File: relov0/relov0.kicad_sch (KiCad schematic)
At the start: 0 parts

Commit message: agregar archivos de kicad a gitignore
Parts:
- added C1, C6: 47u, symbol Device:C_Polarized
- added C2: 100u, symbol Device:C_Polarized
- added C3: 100n, Capacitor_THT:C_Disc_D5.0mm_W2.5mm_P2.50mm, symbol Device:C
- added C4: 10u, symbol Device:C_Polarized
- added C5: 100n, symbol Device:C
- added D1: 1N4007, Diode_THT:D_DO-41_SOD81_P10.16mm_Horizontal, symbol Diode:1N4007
- added D2, D3: LED, symbol Device:LED
- added J1, J2: Barrel_Jack_Switch, symbol Connector:Barrel_Jack_Switch
- added J3: salida, symbol Connector_Audio:AudioJack2_SwitchT
- added R1, R2, R3: 1k, symbol Device:R
- added RV1: 100k, symbol Device:R_Potentiometer
- added SW1: SW_SPDT, symbol Switch:SW_SPDT
- added U1: NE555P, Package_DIP:DIP-8_W7.62mm, symbol Timer:NE555P
- added U2: L7805, symbol Regulator_Linear:L7805
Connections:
- new net: D3.1 (K), R3.1
- new net: C6.1, R2.1, U1.3 (OUT)
- new net: D2.2 (A), R2.2
- new net: D1.2 (A), SW1.2 (B)
- new net: C1.1, RV1.3, U1.2 (TRIG), U1.6 (THRES)
- new net: C3.2, U1.5 (CONT)
- new net: R1.1, RV1.2, U1.7 (DISCH)
- new net: J1.1, J2.1, SW1.1 (A)
- new net +12V: C2.1, D1.1 (K), U2.1 (IN)
- new net +5V: C4.1, C5.1, D3.2 (A), R1.2, U1.4 (~{RST}), U1.8 (VCC), U2.3 (OUT)
- new net GND: C1.2, C2.2, C3.1, C4.2, C5.2, D2.1 (K), J1.2, J2.2, R3.2, U1.1 (GND), U2.2 (GND)
- no-connect marks 0 -> 3
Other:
- note added: "chip 555 1 - conectada a tierra 2 - conectada a 6 3 - conectada a tierra a través de un LED protegido por un resistor, y a salida a través de un capacitor 4 - conectada a vcc 5 - conectada a tierra a través de un capacitor 6 - conectada a 2 7 - conectada a vcc a través de un resistor, y a 2 a través de un resistor 8 - conectada a vcc"
- company: (none) -> piruetas SpA
- title: (none) -> relo

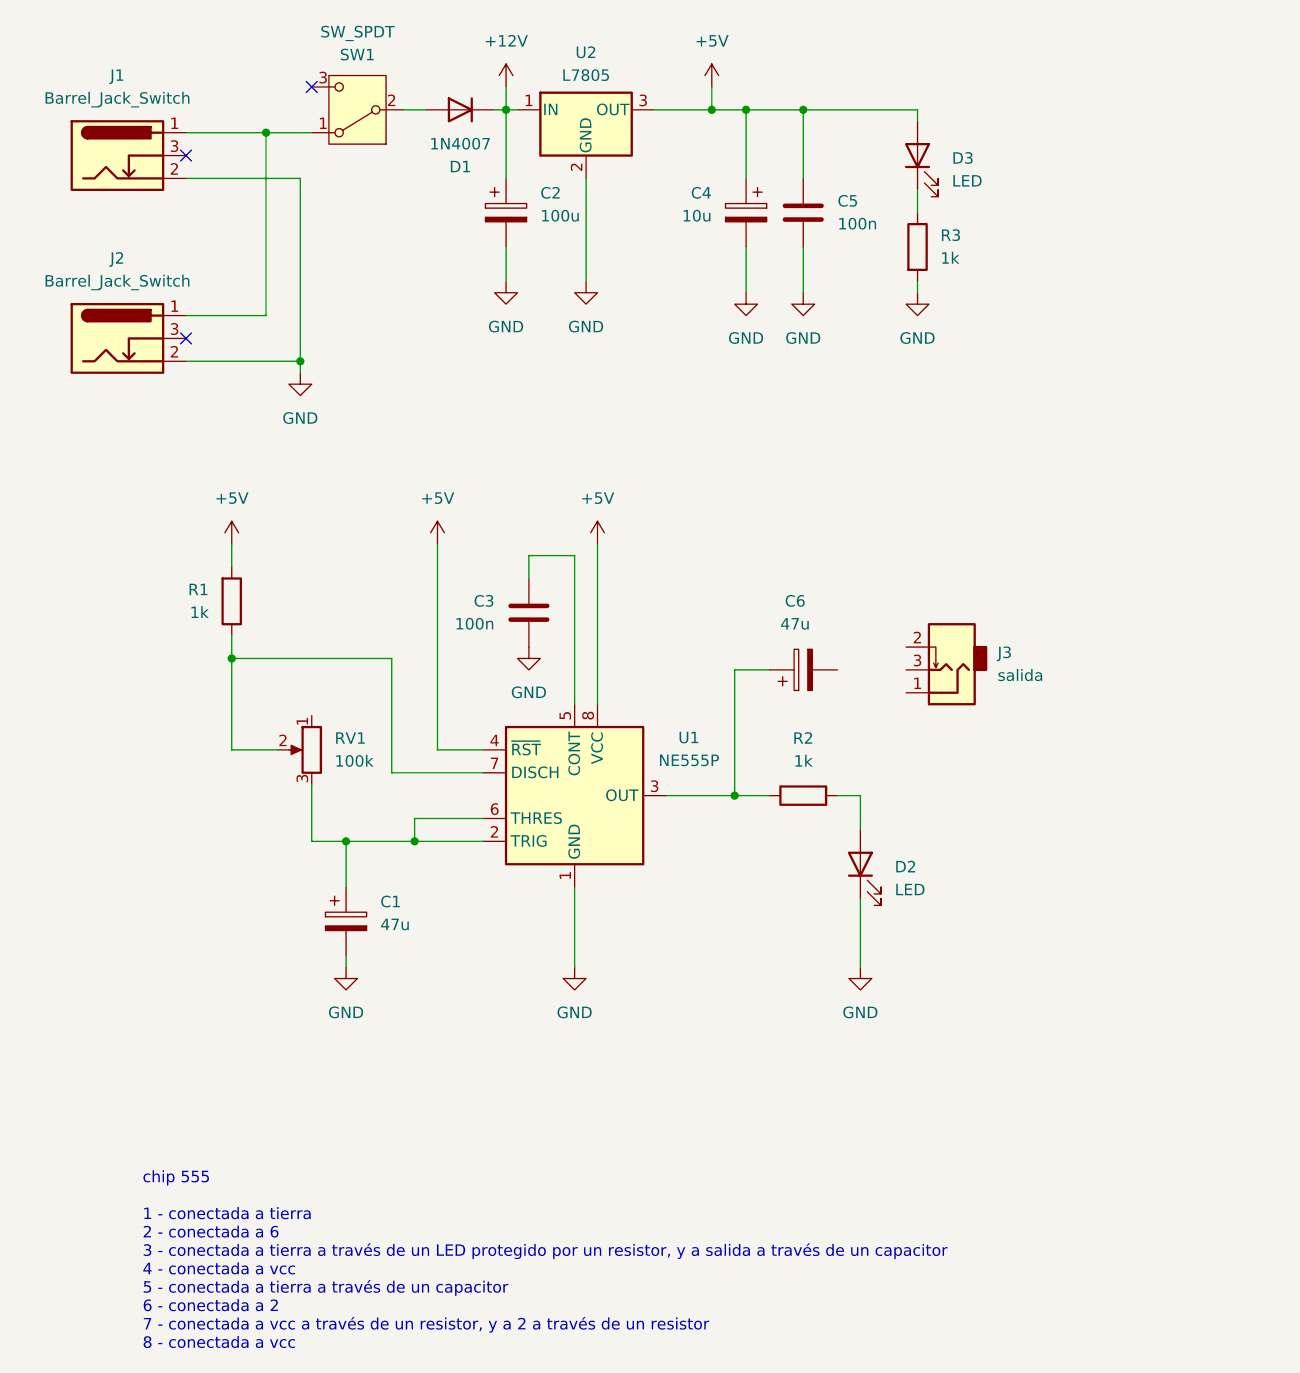
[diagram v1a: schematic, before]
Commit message: agregar biblioteca relo y actualizar footprints
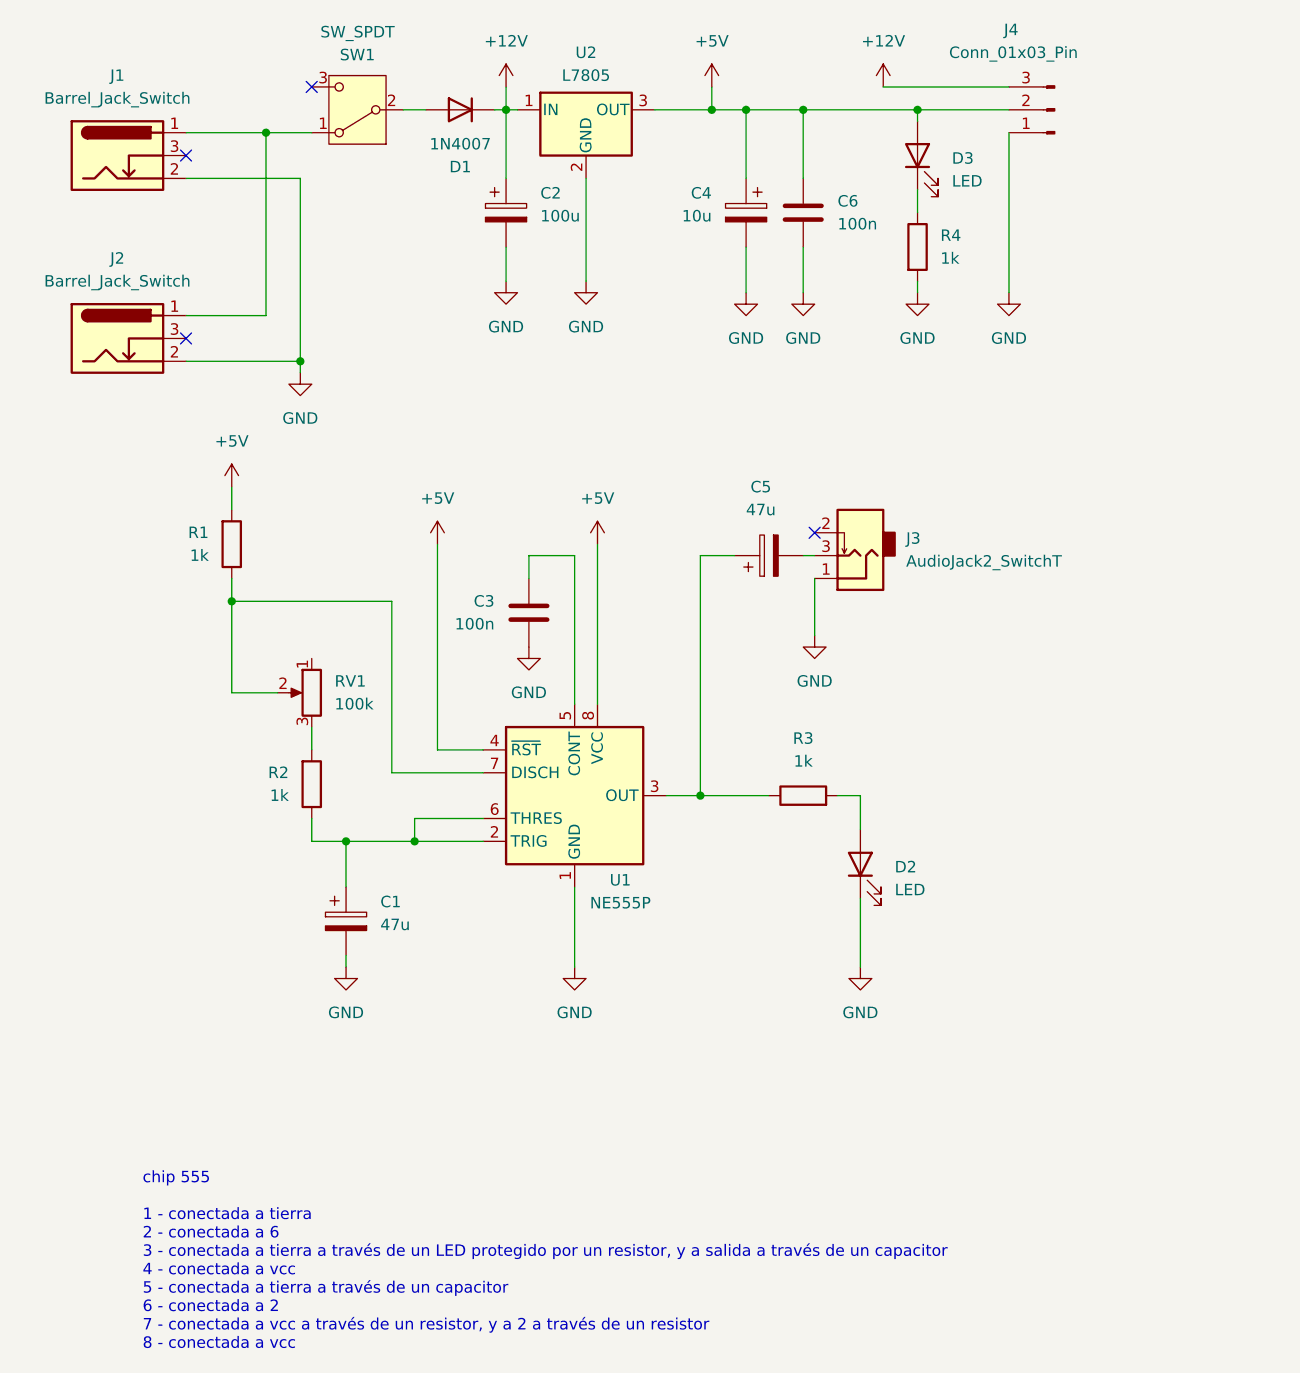
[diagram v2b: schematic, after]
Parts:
- added J4: Conn_01x03_Pin, Connector_PinSocket_2.54mm:PinSocket_1x03_P2.54mm_Vertical, symbol Connector:Conn_01x03_Pin
- added R2: 1k, Resistor_THT:R_Axial_DIN0207_L6.3mm_D2.5mm_P10.16mm_Horizontal, symbol Device:R
- C1: footprint (none) -> Capacitor_THT:CP_Radial_D5.0mm_P2.00mm
- C2: footprint (none) -> Capacitor_THT:CP_Radial_D8.0mm_P3.80mm
- C4: footprint (none) -> Capacitor_THT:CP_Radial_D4.0mm_P2.00mm
- C5: renamed from C6; footprint (none) -> Capacitor_THT:CP_Radial_D5.0mm_P2.00mm
- C6: renamed from C5; footprint (none) -> Capacitor_THT:C_Disc_D5.0mm_W2.5mm_P2.50mm
- D2, D3: footprint (none) -> LED_THT:LED_D5.0mm
- J1, J2: footprint (none) -> Connector_BarrelJack:BarrelJack_Horizontal
- J3: value salida -> AudioJack2_SwitchT; footprint (none) -> relo:PJ301M-12
- R1: footprint (none) -> Resistor_THT:R_Axial_DIN0207_L6.3mm_D2.5mm_P10.16mm_Horizontal
- R3: renamed from R2; footprint (none) -> Resistor_THT:R_Axial_DIN0207_L6.3mm_D2.5mm_P10.16mm_Horizontal
- R4: renamed from R3; footprint (none) -> Resistor_THT:R_Axial_DIN0207_L6.3mm_D2.5mm_P10.16mm_Horizontal
- RV1: footprint (none) -> Potentiometer_THT:Potentiometer_Alps_RK163_Single_Horizontal
- SW1: footprint (none) -> Button_Switch_THT:SW_Slide_SPDT_Straight_CK_OS102011MS2Q
- U1: footprint Package_DIP:DIP-8_W7.62mm -> Package_DIP:DIP-8_W7.62mm_Socket_LongPads
- U2: footprint (none) -> Package_TO_SOT_THT:TO-220-3_Horizontal_TabDown
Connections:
- net +12V: now also J4.3 (Pin_3)
- net +5V: now also J4.2 (Pin_2)
- net GND: now also J3.1, J4.1 (Pin_1)
- net at C1.1, U1.2 (TRIG), U1.6 (THRES): now also R2.1; no longer RV1.3
- net at C5.2: now also J3.3
- new net: R2.2, RV1.3
- no-connect marks 3 -> 4
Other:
- moved on the sheet: C5, J3, R1, RV1

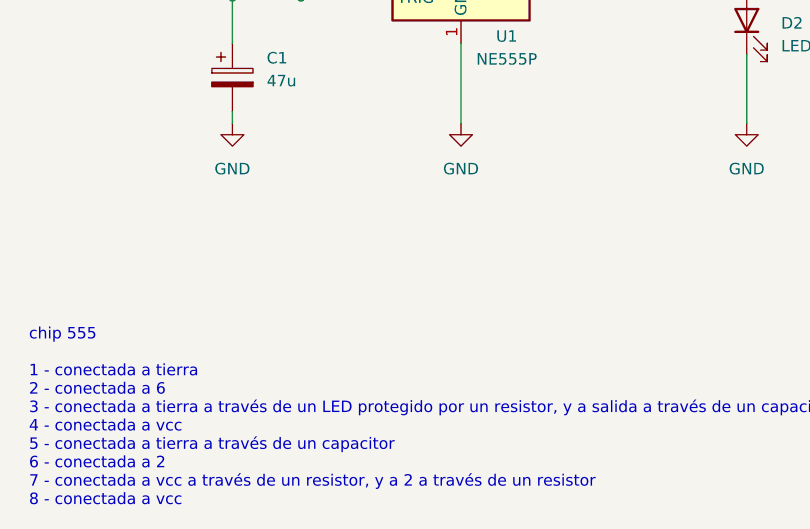
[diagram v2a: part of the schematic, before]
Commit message: agregar nuevas mods
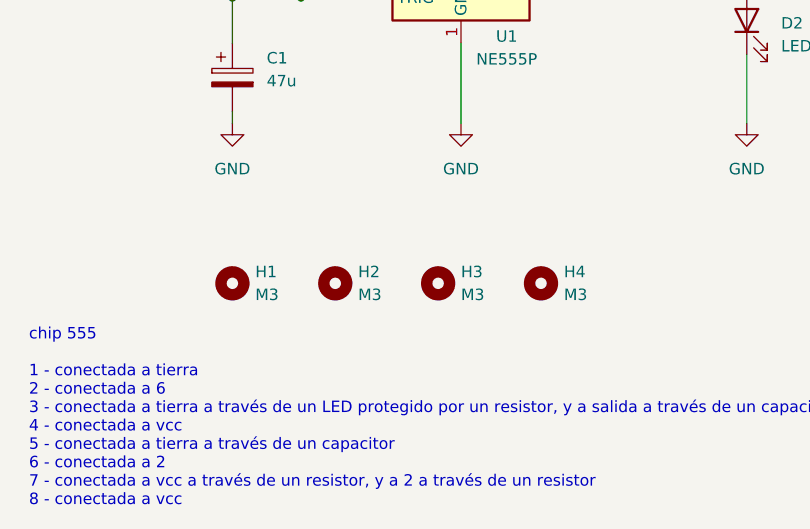
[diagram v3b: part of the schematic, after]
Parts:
- added H1, H2, H3, H4: M3, MountingHole:MountingHole_3.2mm_M3, symbol Mechanical:MountingHole

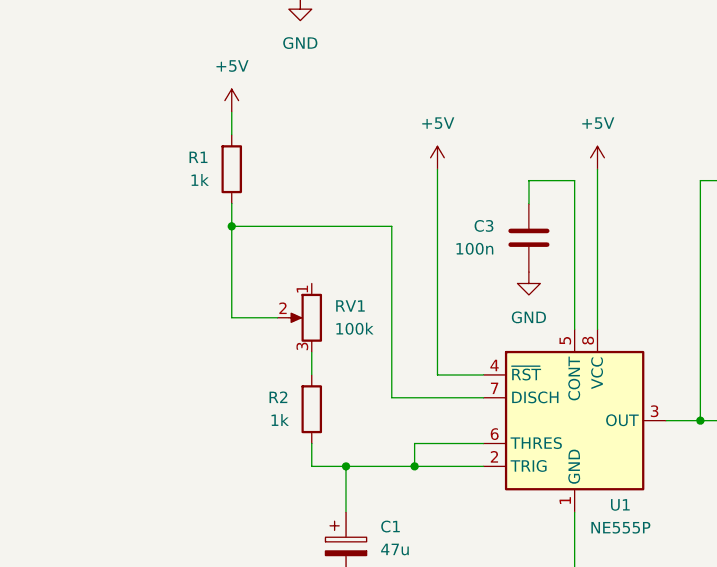
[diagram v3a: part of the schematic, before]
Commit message: agregar vias
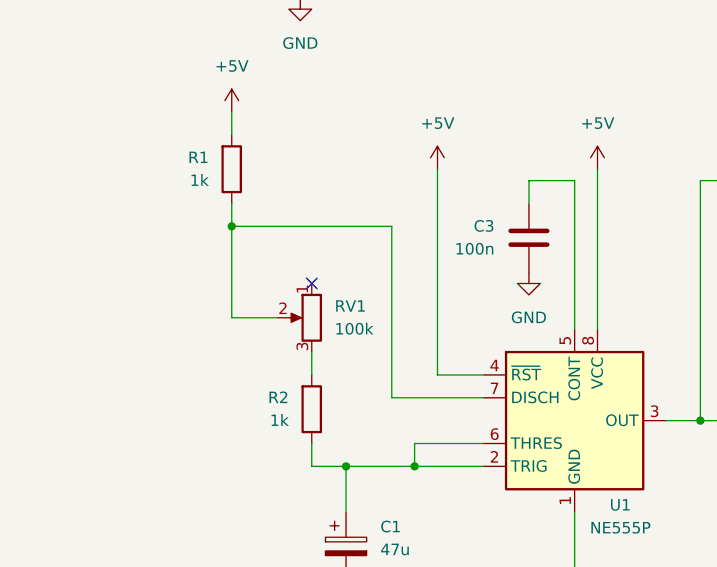
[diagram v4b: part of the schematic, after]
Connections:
- no-connect marks 4 -> 5
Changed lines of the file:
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@@
+	)
+	(no_connect
+		(at 46.99 86.36)
 	)
 	(no_connect

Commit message: añadido gerb
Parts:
- C5: value 47u -> 220u
- SW1: footprint Button_Switch_THT:SW_Slide_SPDT_Straight_CK_OS102011MS2Q -> dis8644:spdt_ssd12d00g3
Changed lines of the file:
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@@
 			)
 		)
-		(property "Value" "47u"
+		(property "Value" "220u"
 			(at 96.901 69.85 90)
 			(show_name no)
@@
 			)
 		)
-		(property "Footprint" "Button_Switch_THT:SW_Slide_SPDT_Straight_CK_OS102011MS2Q"
+		(property "Footprint" "dis8644:spdt_ssd12d00g3"
 			(at 52.07 25.4 0)
 			(hide yes)
